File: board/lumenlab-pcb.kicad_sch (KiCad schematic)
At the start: 26 parts, among them J1 2.1mm Barrel Jack, SW1 SW_SPST, U1 MP2338, U2 AMS1117, U3 ESP32-WROOM-32D

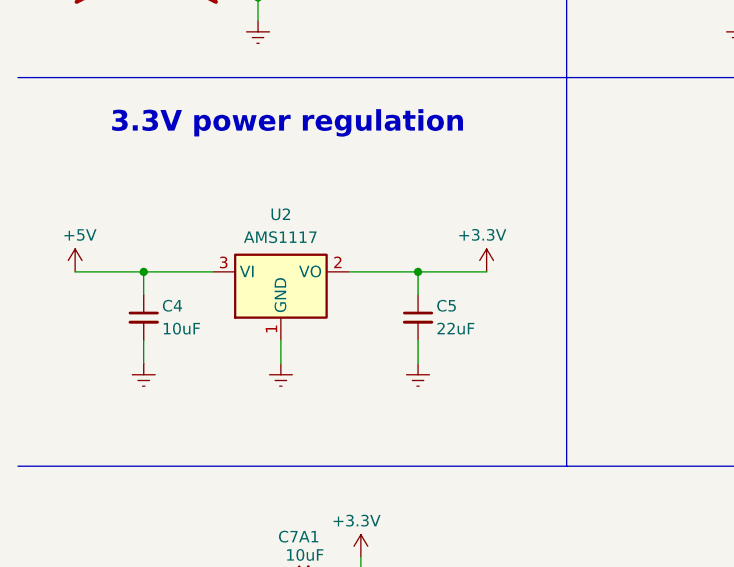
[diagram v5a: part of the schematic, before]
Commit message: Replace AMS1117 with AP7361C
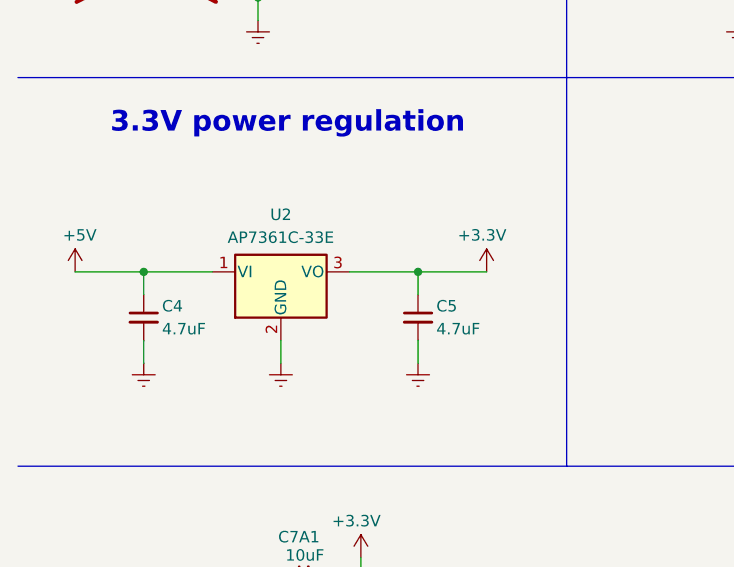
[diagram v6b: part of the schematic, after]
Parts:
- removed U2: AMS1117, Package_TO_SOT_SMD:SOT-223-3_TabPin2, symbol Regulator_Linear:AMS1117-3.3
- added U2: AP7361C-33E, Package_TO_SOT_SMD:SOT-223-3_TabPin2, symbol Regulator_Linear:AP7361C-33E
- C4: value 10uF -> 4.7uF
- C5: value 22uF -> 4.7uF
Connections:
- net +3.3V: now also U2.3 (VO)
- net +5V: now also U2.1 (VI)
- net GND: now also U2.2 (GND)
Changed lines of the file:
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@@
 			)
 		)
-		(property "Value" "10uF"
+		(property "Value" "4.7uF"
 			(at 28.702 73.66 0)
 			(effects
@@
 				(path "/2d045da9-3430-412d-9b59-c1acb2d29754"
 					(reference "L1")
+					(unit 1)
+				)
+			)
+		)
+	)
+	(symbol
+		(lib_id "Regulator_Linear:AP7361C-33E")
+		(at 41.91 67.31 0)
+		(unit 1)
+		(exclude_from_sim no)
+		(in_bom yes)
+		(on_board yes)
+		(dnp no)
+		(fields_autoplaced yes)
+		(property "Reference" "U2"
+			(at 41.91 60.96 0)
+			(effects
+				(font
+					(size 1.27 1.27)
+				)
+			)
+		)
+		(property "Value" "AP7361C-33E"
+			(at 41.91 63.5 0)
+			(effects
+				(font
+					(size 1.27 1.27)
+				)
+			)
+		)
+		(property "Footprint" "Package_TO_SOT_SMD:SOT-223-3_TabPin2"
+			(at 41.91 61.595 0)
+			(effects
+				(font
+					(size 1.27 1.27)
+					(italic yes)
+				)
+				(hide yes)
+			)
+		)
+		(property "Datasheet" "https://www.diodes.com/assets/Datasheets/AP7361C.pdf"
+			(at 41.91 68.58 0)
+			(effects
+				(font
+					(size 1.27 1.27)
+				)
+				(hide yes)
+			)
+		)
+		(property "Description" "1A Low Dropout regulator, positive, 3.3V fixed output, SOT-223"
+			(at 41.91 67.31 0)
+			(effects
+				(font
+					(size 1.27 1.27)
+				)
+				(hide yes)
+			)
+		)
+		(pin "1"
+		)
+		(pin "2"
+		)
+		(pin "3"
+		)
+		(instances
+			(project ""
+				(path "/2d045da9-3430-412d-9b59-c1acb2d29754"
+					(reference "U2")
 					(unit 1)
 				)
@@
 			)
 		)
-		(property "Value" "22uF"
+		(property "Value" "4.7uF"
 			(at 59.182 73.66 0)
 			(effects
@@
 					(unit 1)
 				)
-			)
-		)
-	)
-	(symbol
-		(lib_id "Regulator_Linear:AMS1117-3.3")
-		(at 41.91 67.31 0)
-		(unit 1)
-		(exclude_from_sim no)
-		(in_bom yes)
-		(on_board yes)
-		(dnp no)
-		(fields_autoplaced yes)
-		(property "Reference" "U2"
-			(at 41.91 60.96 0)
-			(effects
-				(font
-					(size 1.27 1.27)
-				)
-			)
-		)
-		(property "Value" "AMS1117"
-			(at 41.91 63.5 0)
-			(effects
-				(font
-					(size 1.27 1.27)
-				)
-			)
-		)
-		(property "Footprint" "Package_TO_SOT_SMD:SOT-223-3_TabPin2"
-			(at 41.91 62.23 0)
-			(effects
-				(font
-					(size 1.27 1.27)
-				)
-				(hide yes)
-			)
-		)
-		(property "Datasheet" "http://www.advanced-monolithic.com/pdf/ds1117.pdf"
-			(at 44.45 73.66 0)
-			(effects
-				(font
-					(size 1.27 1.27)
-				)
-				(hide yes)
-			)
-		)
-		(property "Description" "1A Low Dropout regulator, positive, 3.3V fixed output, SOT-223"
-			(at 41.91 67.31 0)
-			(effects
-				(font
-					(size 1.27 1.27)
-				)
-				(hide yes)
-			)
-		)
-		(pin "2"
-		)
-		(pin "3"
-		)
-		(pin "1"
-		)
-		(instances
-			(project ""
-				(path "/2d045da9-3430-412d-9b59-c1acb2d29754"
-					(reference "U2")
-					(unit 1)
-				)
